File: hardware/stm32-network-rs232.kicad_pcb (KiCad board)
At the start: 2 copper layers, 53 parts, among them J1 USB, M1 Mount Hole, M2 Mount Hole, M3 Mount Hole, M4 Mount Hole, P2 P10, P3 DEBUG, P4 SWD, P5 RS232-TAP, U1 ENC28J60, U2 STM32-48PIN, U4 MOSFET-P, U5 ZLDO1117, X1 25MHz, X2 8MHz

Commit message: initial layout
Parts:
- removed C17: 0.1uF, kicad-lib:CAPC2012X100N
- added C26: 10uF, kicad-lib:CAPCP2012X100N, F.Cu at (82.0, 84.0)
- added L1: >80mA, kicad-lib:RESC2012X100N, F.Cu at (86.0, 69.5)
- added P1: BELFUSE-08B0-1X1T-06-F, kicad-lib:BEL-FUSE-08B0-1X1T-06-F, F.Cu at (72.5, 68.0)
- added P6: RS-232-DB-9-DTE, kicad-lib:TECONN-5747840-2, F.Cu at (131.5, 74.0)
- added P7: P03, kicad-lib:HDRV3W66P254_1X3_762X249X838P, F.Cu at (123.5, 62.5)
- added P8: P03, kicad-lib:HDRV3W66P254_1X3_762X249X838P, F.Cu at (123.5, 65.5)
- added U3: MAX3221, kicad-lib:SOP65P640X120-16N, F.Cu at (115.5, 71.5)
- C25: footprint kicad-lib:CAPC2012X100N -> kicad-lib:CAPCP2012X100N
- moved M1 144.2 mm to (55.0, 55.0)
- moved R12 143.6 mm to (64.0, 89.0), turned to 270 degrees
- moved R11 143.3 mm to (60.0, 88.0), turned to 180 degrees
- moved R8 142.7 mm to (60.0, 93.5)
- moved R10 139.6 mm to (60.0, 85.5), turned to 180 degrees
- moved C23 139.0 mm to (60.0, 90.5), turned to 180 degrees
- moved R3 138.7 mm to (81.5, 59.5)
- moved U4 138.1 mm to (68.0, 89.0)
- moved C24 135.1 mm to (60.0, 83.0), turned to 180 degrees
- moved R9 132.7 mm to (68.0, 85.5)
- moved R6 132.6 mm to (81.5, 62.0)
- moved C14 131.3 mm to (81.5, 64.5)
- moved R5 130.3 mm to (81.5, 69.5)
- moved C3 127.2 mm to (88.5, 55.5), turned to 270 degrees
- moved R7 127.2 mm to (81.5, 67.0)
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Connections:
- J1 pad 1: +3.3V -> +5V
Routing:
- added copper zone on F.Cu, net GNDPWR
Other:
- board outline added: 105 x 50 mm

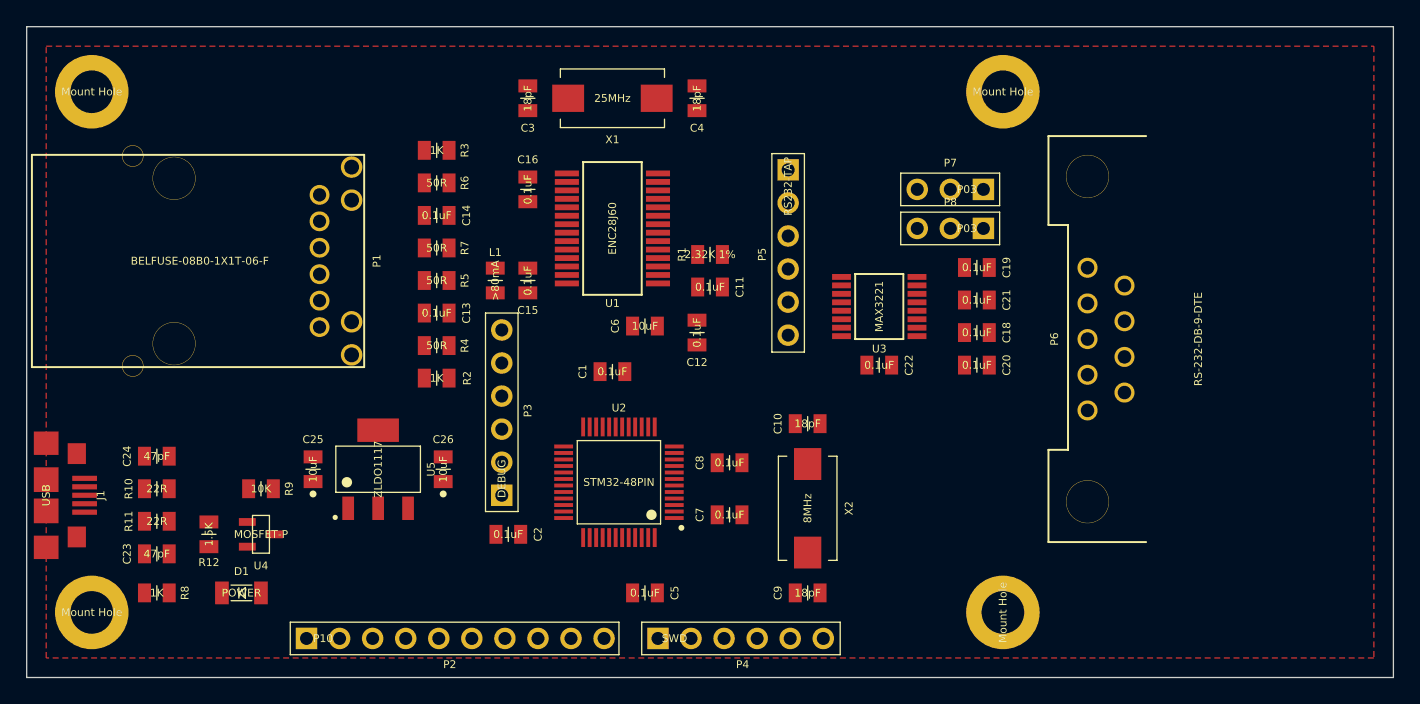
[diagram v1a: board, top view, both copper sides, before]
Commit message: upgrade to new modules part 1
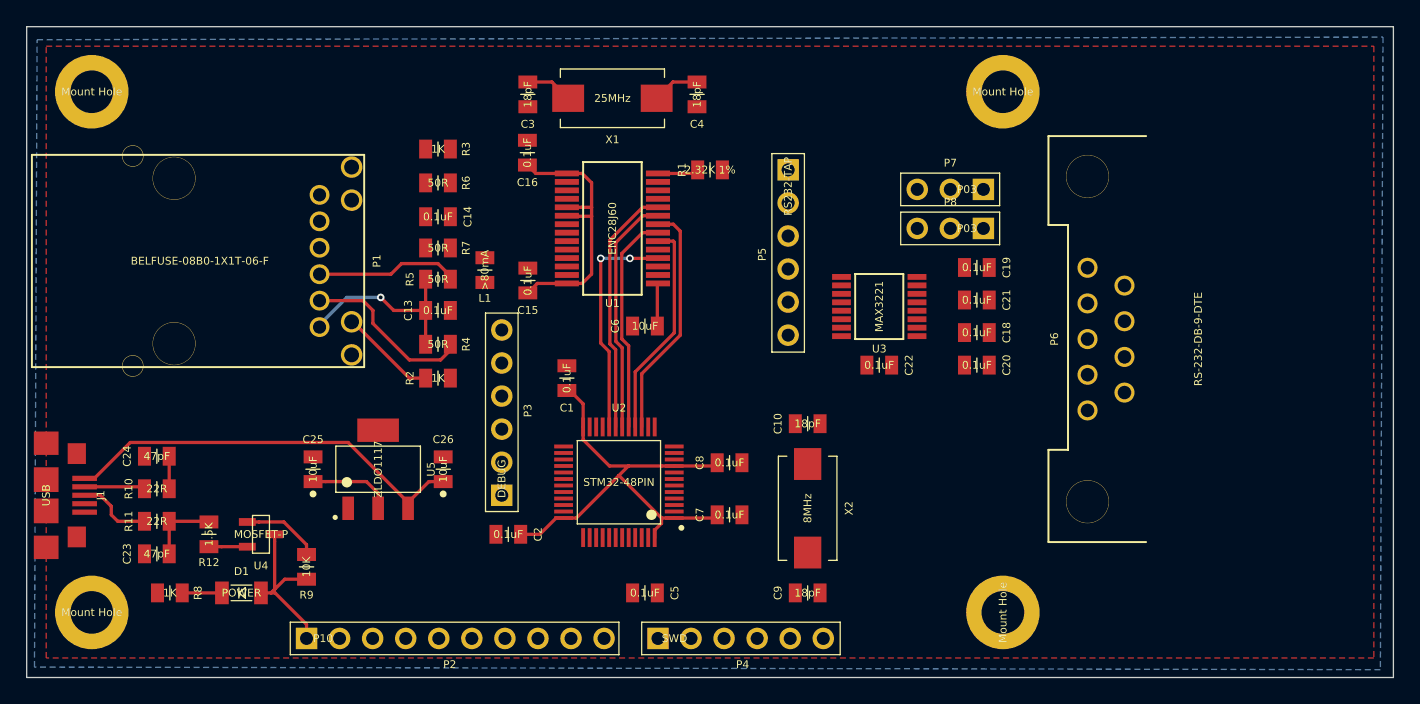
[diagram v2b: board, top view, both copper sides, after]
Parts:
- removed C11, C12: 0.1uF, kicad-lib:CAPC2012X100N
- C1, C10, C13, C14, C15, C16, C18, C19, C2, C20, C21, C22, C23, C24, C3, C4, C5, C6, C7, C8, C9: footprint kicad-lib:CAPC2012X100N -> kicad-new-lib:CAPC2012X100N
- C25, C26: footprint kicad-lib:CAPCP2012X100N -> kicad-new-lib:CAPCP2012X100N
- D1: footprint kicad-lib:LEDC3216X100N -> kicad-new-lib:LEDC3216X100N
- J1: footprint kicad-lib:JST_UB-MC5BR3-SD204-4S-NMP -> kicad-new-lib:JST_UB-MC5BR3-SD204-4S-NMP
- L1, R1, R10, R11, R12, R2, R3, R4, R5, R6, R7, R8, R9: footprint kicad-lib:RESC2012X100N -> kicad-new-lib:RESC2012X100N
- M1, M2, M3, M4: footprint kicad-lib:MTGNP565H328Z565P -> kicad-new-lib:MTGNP565H328Z565P
- P1: footprint kicad-lib:BEL-FUSE-08B0-1X1T-06-F -> kicad-new-lib:BEL-FUSE-08B0-1X1T-06-F
- P2: footprint kicad-lib:HDRV10W66P254_1X10_1006X249X838P -> kicad-new-lib:HDRV10W66P254_1X10_1006X249X838P
- P3, P4, P5: footprint kicad-lib:HDRV6W66P254_1X6_1524X249X838P -> kicad-new-lib:HDRV6W66P254_1X6_1524X249X838P
- P6: footprint kicad-lib:TECONN-5747840-2 -> kicad-new-lib:TECONN-5747840-2
- P7, P8: footprint kicad-lib:HDRV3W66P254_1X3_762X249X838P -> kicad-new-lib:HDRV3W66P254_1X3_762X249X838P
- U1: footprint kicad-lib:SOP65P780X200-28N -> kicad-new-lib:SOP65P780X200-28N
- U2: footprint kicad-lib:QFP50P900X900X160-48N -> kicad-new-lib:QFP50P900X900X160-48N
- U3: footprint kicad-lib:SOP65P640X120-16N -> kicad-new-lib:SOP65P640X120-16N
- U4: footprint kicad-lib:SOT95P237X112_123-3N -> kicad-new-lib:SOT95P237X112_123-3N
- U5: footprint kicad-lib:SOT230P700X180-4N -> kicad-new-lib:SOT230P700X180-4N
- X1, X2: footprint kicad-lib:XTAL8045X200N -> kicad-new-lib:XTAL8045X200N
- moved R9 6.95 mm to (71.5, 91.5), turned to 270 degrees
- moved R1 6.50 mm to (102.5, 61.0)
- moved C1 3.54 mm to (91.5, 77.0), turned to 270 degrees
- moved C16 2.82 mm to (88.5, 59.7), turned to 270 degrees
- moved L1 1.13 mm to (85.2, 68.7), turned to 270 degrees
- moved R8 1.00 mm to (61.0, 93.5)
- moved C3 0.30 mm to (88.5, 55.2)
- moved C4 0.30 mm to (101.5, 55.2)
- moved C13 0.22 mm to (81.6, 71.8), turned to 180 degrees
- moved R3 0.14 mm to (81.6, 59.4)
- moved C14 0.14 mm to (81.6, 64.6)
- moved R4 0.14 mm to (81.6, 74.4)
- moved R5 0.14 mm to (81.6, 69.4), turned to 180 degrees
- moved R2 0.10 mm to (81.6, 77.0)
- moved R6 0.10 mm to (81.6, 62.0)
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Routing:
- net +3.3V: track 0.00 -> 79.1 mm
- net +5V: track 0.00 -> 31.7 mm
- net /ENC28J60RESET: track 0.00 -> 19.3 mm
- net /ENC28J60CS: track 0.00 -> 18.5 mm
- net /SPISCK: track 0.00 -> 18.2 mm
- net /ENC28J60INT: track 0.00 -> 17.6 mm, vias 0 -> 2
- net /SPIMOSI: track 0.00 -> 17.0 mm
- net /SPIMISO: track 0.00 -> 16.7 mm
- net Net-(C13-Pad2): track 0.00 -> 14.6 mm, vias 0 -> 1
- net Net-(P1-Pad2): track 0.00 -> 13.5 mm
- net Net-(P1-Pad3): track 0.00 -> 11.0 mm
- net Net-(P1-Pad8): track 0.00 -> 7.48 mm
- net /USBDIS: track 0.00 -> 6.03 mm
- net Net-(J1-Pad3): track 0.00 -> 5.81 mm
- net /USBDP: track 0.00 -> 5.57 mm
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- added copper zone on B.Cu, net GNDPWR
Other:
- net class Default: clearance 0.254 -> 0.2032; via_dia 0.889 -> 0.5842; via_drill 0.635 -> 0.3302
- rule trace_clearance: 0.254 -> 0.2032
- rule trace_min: 0.254 -> 0.2032
- rule via_min_drill: 0.508 -> 0.3302
- rule via_min_size: 0.889 -> 0.508

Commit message: board routing
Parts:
- moved C4 17.3 mm to (97.2, 72.0), turned to 180 degrees
- moved C3 17.0 mm to (91.0, 72.0), turned to 0 degrees
- moved R1 16.2 mm to (86.8, 57.2), turned to 90 degrees
- moved C6 16.1 mm to (100.8, 57.2), turned to 270 degrees
- moved P7 15.0 mm to (108.5, 62.5), turned to 0 degrees
- moved X1 12.5 mm to (94.0, 68.0)
- moved C15 12.1 mm to (100.4, 67.2), turned to 90 degrees
- moved P8 9.97 mm to (113.5, 65.0)
- moved C20 5.69 mm to (117.4, 75.0)
- moved P6 5.69 mm to (125.9, 75.0)
- moved C18 5.66 mm to (117.4, 72.7)
- moved C21 5.63 mm to (117.4, 70.4)
- moved C19 5.61 mm to (117.4, 68.1)
- moved U1 5.43 mm to (93.8, 60.2), turned to 270 degrees
- moved P5 4.84 mm to (104.3, 63.4)
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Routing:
- net +3.3V: track 79.1 -> 154.2 mm, vias 0 -> 2
- net GNDPWR: track 0.00 -> 55.5 mm, vias 0 -> 19
- net Net-(P2-Pad5): track 0.00 -> 33.1 mm, vias 0 -> 1
- net Net-(R3-Pad1): track 0.00 -> 32.6 mm
- net /USBDM: track 2.50 -> 35.1 mm
- net /USBDP: track 5.57 -> 35.0 mm
- net Net-(P2-Pad3): track 0.00 -> 28.6 mm, vias 0 -> 2
- net /SWDIO: track 0.00 -> 27.2 mm, vias 0 -> 2
- net Net-(R2-Pad1): track 0.00 -> 27.1 mm, vias 0 -> 2
- net Net-(P2-Pad6): track 0.00 -> 26.6 mm, vias 0 -> 1
- net Net-(P1-Pad4): track 0.00 -> 26.5 mm, vias 0 -> 2
- net /USBDIS: track 6.03 -> 31.5 mm, vias 0 -> 2
- net Net-(P2-Pad4): track 0.00 -> 25.3 mm, vias 0 -> 2
- net Net-(P1-Pad5): track 0.00 -> 25.2 mm, vias 0 -> 1
- net Net-(P2-Pad7): track 0.00 -> 22.9 mm, vias 0 -> 2
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
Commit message: board layout complete
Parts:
- moved M3 6.60 mm to (131.6, 95.0)
- moved M4 6.60 mm to (131.6, 55.0)
- moved M1 1.40 mm to (53.6, 55.0)
- moved M2 1.40 mm to (53.6, 95.0)
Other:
- board size 105 x 50 mm -> 85.2 x 47.2 mm
- board text added: "+3.3V"
- board text added: "2014-07-12"
- board text added: "By: Joe Ferner"
- board text added: "DCE"
- board text added: "DEBUG"
- board text added: "DTE"
- board text added: "GND"
- board text added: "Network <-> RS232"
- board text added: "PB10"
- board text added: "PB11"
- board text added: "PB12"
- board text added: "PB13"
- board text added: "PB14"
- board text added: "PB15"
- board text added: "PB8"
- board text added: "PB9"
- board text added: "POWER"
- board text added: "RX"
- board text added: "SWD"
- board text added: "TX"
- board text added: "USART"

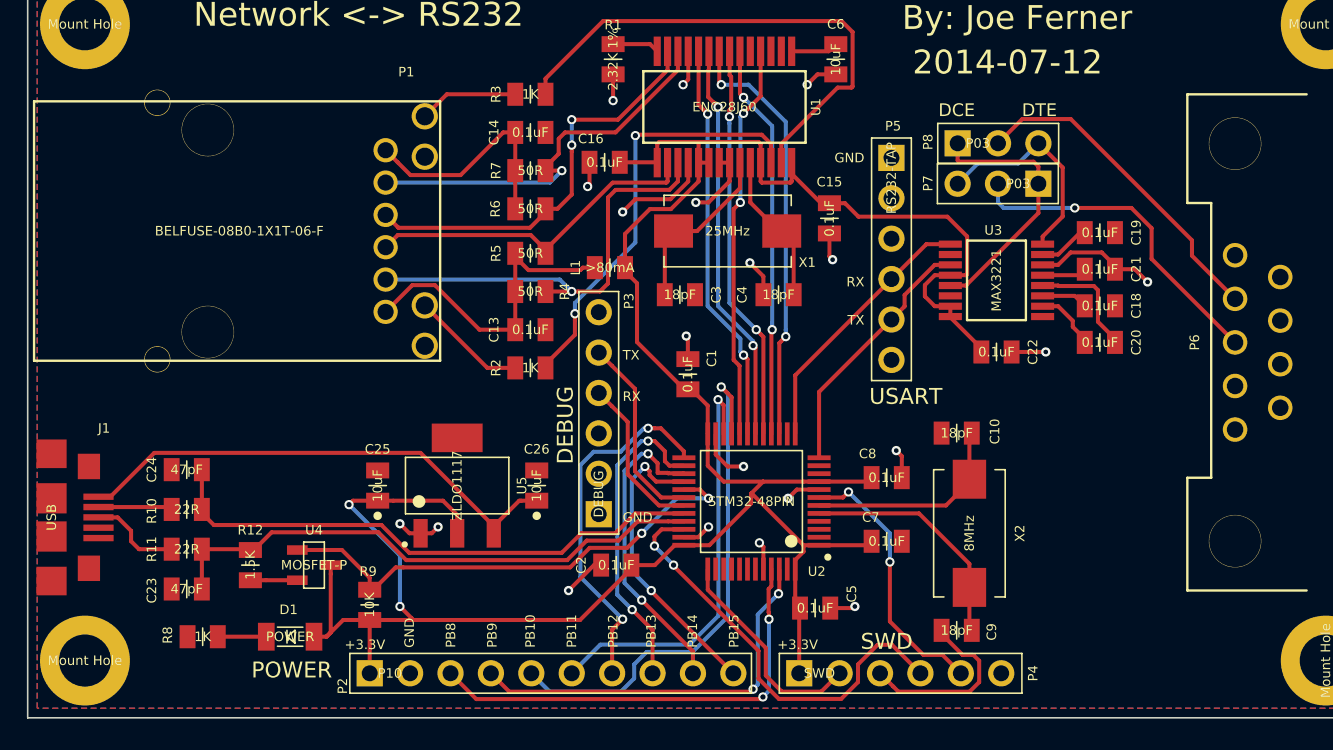
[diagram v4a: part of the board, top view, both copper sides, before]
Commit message: increase power trace widths
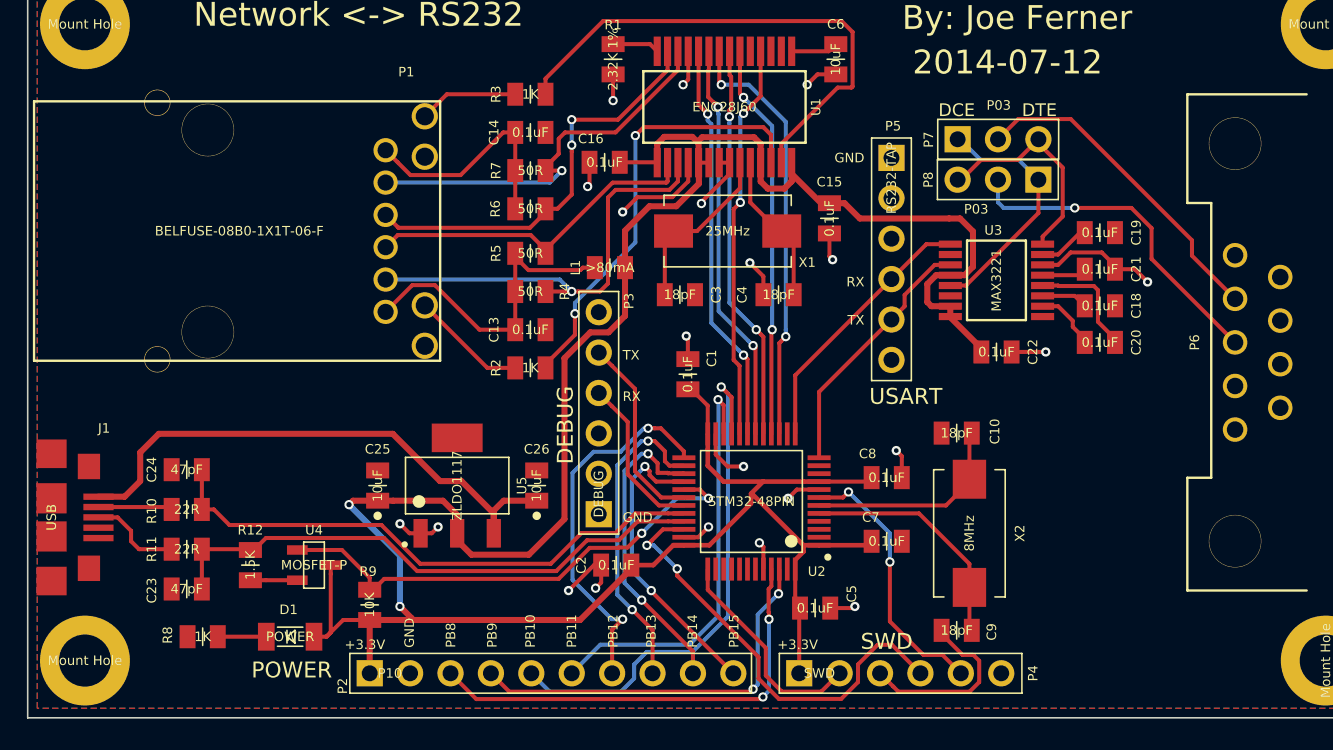
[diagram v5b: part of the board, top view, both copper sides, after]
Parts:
- moved P7 0.25 mm to (108.5, 62.2)
- moved P8 0.25 mm to (113.5, 64.8)
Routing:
- net +3.3V: track 153.9 -> 173.7 mm
- net +5V: track 31.7 -> 36.5 mm
- net GNDPWR: track 55.5 -> 56.6 mm, vias 19 -> 20
- net /RS232TX: track 16.7 -> 15.7 mm
- net Net-(P2-Pad7): track 22.9 -> 23.7 mm
- net Net-(R2-Pad1): track 27.1 -> 27.9 mm
- net /SWDIO: track 27.2 -> 27.8 mm
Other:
- net class power added: clearance 0.2032, trace_width 0.381, via_dia 0.5842, via_drill 0.3302
- net class powersmall added: clearance 0.2032, trace_width 0.2921, via_dia 0.5842, via_drill 0.3302
